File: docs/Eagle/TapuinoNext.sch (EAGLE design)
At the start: 8 parts

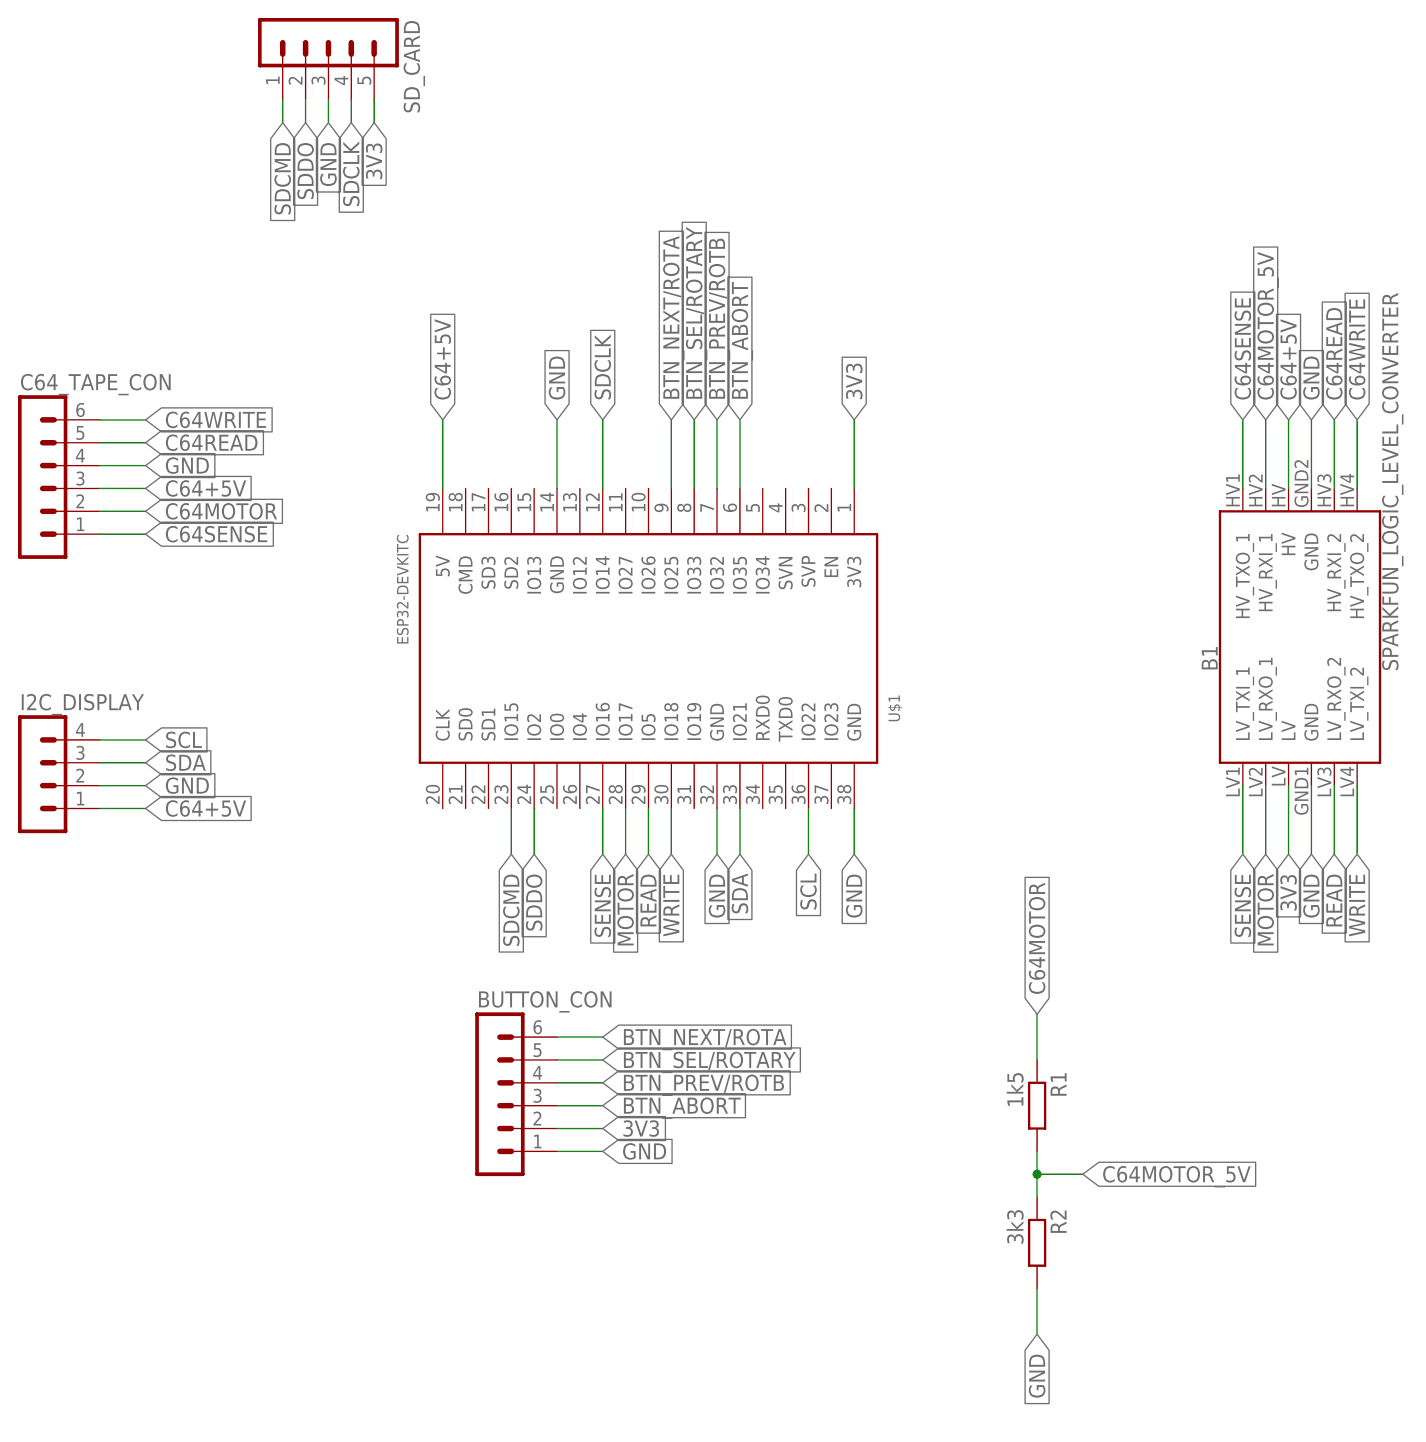
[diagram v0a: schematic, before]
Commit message: add rec led and tidied up the board / schematic
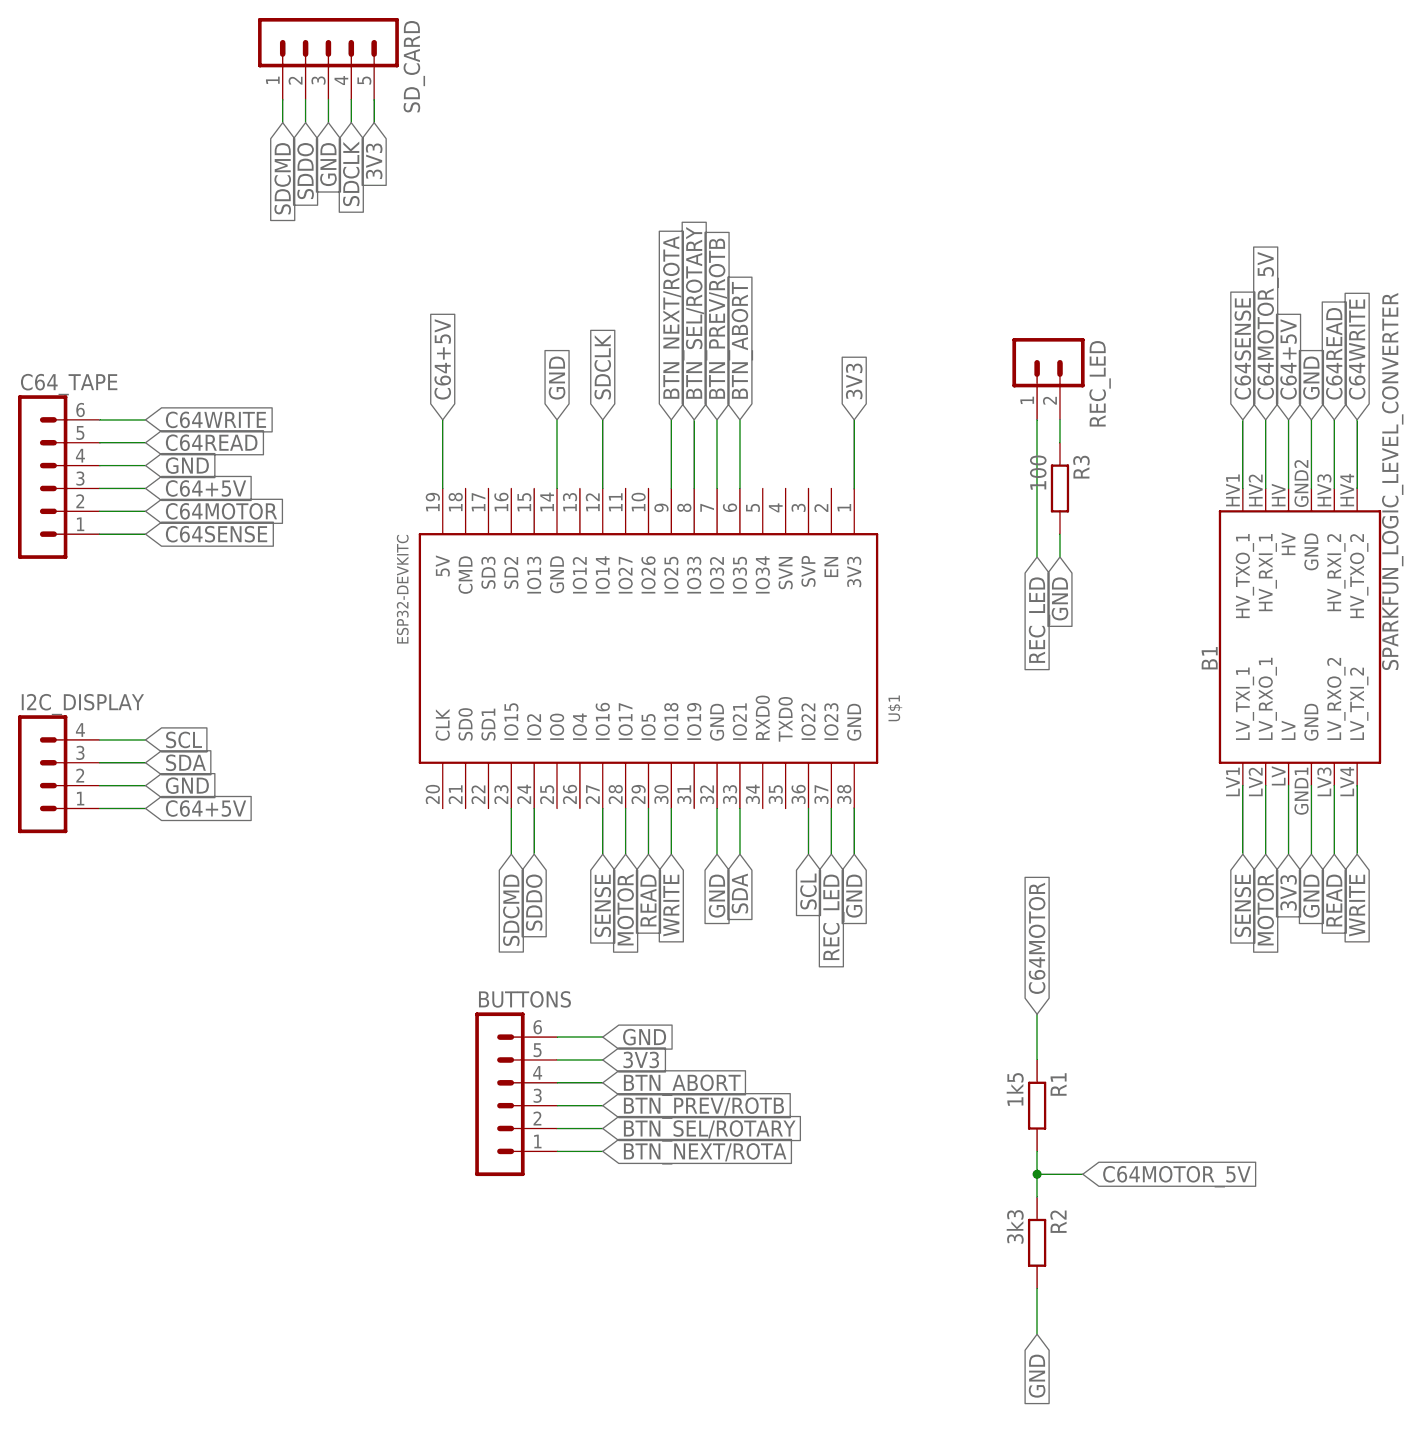
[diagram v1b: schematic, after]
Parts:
- added R3: 100, rcl:R-EU_0204/7
- added REC_LED: (no value), con-lstb-ext:MA02-1
- renumbered BUTTON_CON to BUTTONS, C64_TAPE_CON to C64_TAPE
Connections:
- new net N$2: R3.1, REC_LED.2
- new net REC_LED: REC_LED.1, U$1.IO23
- net 3V3: now also BUTTONS.5; no longer BUTTONS.2
- net BTN_ABORT: now also BUTTONS.4; no longer BUTTONS.3
- net BTN_NEXT/ROTA: now also BUTTONS.1; no longer BUTTONS.6
- net BTN_PREV/ROTB: now also BUTTONS.3; no longer BUTTONS.4
- net BTN_SEL/ROTARY: now also BUTTONS.2; no longer BUTTONS.5
- net GND: now also BUTTONS.6, R3.2; no longer BUTTONS.1
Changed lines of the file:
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@@
 <part name="U$1" library="ESP32-DEVKITC" deviceset="ESP32DEVKITC" device=""/>
 <part name="I2C_DISPLAY" library="con-lstb" library_urn="urn:adsk.eagle:library:162" deviceset="MA04-1" device="" package3d_urn="urn:adsk.eagle:package:8337/1"/>
-<part name="C64_TAPE_CON" library="con-lstb" library_urn="urn:adsk.eagle:library:162" deviceset="MA06-1" device="" package3d_urn="urn:adsk.eagle:package:8340/1"/>
-<part name="BUTTON_CON" library="con-lstb" library_urn="urn:adsk.eagle:library:162" deviceset="MA06-1" device="" package3d_urn="urn:adsk.eagle:package:8340/1"/>
+<part name="C64_TAPE" library="con-lstb" library_urn="urn:adsk.eagle:library:162" deviceset="MA06-1" device="" package3d_urn="urn:adsk.eagle:package:8340/1"/>
+<part name="BUTTONS" library="con-lstb" library_urn="urn:adsk.eagle:library:162" deviceset="MA06-1" device="" package3d_urn="urn:adsk.eagle:package:8340/1"/>
 <part name="R2" library="rcl" library_urn="urn:adsk.eagle:library:334" deviceset="R-EU_" device="0204/7" package3d_urn="urn:adsk.eagle:package:23498/2" value="3k3"/>
 <part name="R1" library="rcl" library_urn="urn:adsk.eagle:library:334" deviceset="R-EU_" device="0204/7" package3d_urn="urn:adsk.eagle:package:23498/2" value="1k5"/>
 <part name="SD_CARD" library="con-lstb" library_urn="urn:adsk.eagle:library:162" deviceset="MA05-1" device="" package3d_urn="urn:adsk.eagle:package:8332/1"/>
+<part name="R3" library="rcl" library_urn="urn:adsk.eagle:library:334" deviceset="R-EU_" device="0204/7" package3d_urn="urn:adsk.eagle:package:23498/2" value="100"/>
+<part name="REC_LED" library="con-lstb-ext" deviceset="MA02-1" device="" package3d_urn="urn:adsk.eagle:package:30404189/1"/>
 </parts>
 <sheets>
@@
 <attribute name="NAME" x="-24.13" y="36.322" size="1.778" layer="95"/>
 </instance>
-<instance part="C64_TAPE_CON" gate="1" x="-22.86" y="63.5" smashed="yes">
+<instance part="C64_TAPE" gate="1" x="-22.86" y="63.5" smashed="yes">
 <attribute name="VALUE" x="-24.13" y="50.8" size="1.778" layer="96"/>
 <attribute name="NAME" x="-24.13" y="71.882" size="1.778" layer="95"/>
 </instance>
-<instance part="BUTTON_CON" gate="1" x="27.94" y="-5.08" smashed="yes">
+<instance part="BUTTONS" gate="1" x="27.94" y="-5.08" smashed="yes">
 <attribute name="VALUE" x="26.67" y="-17.78" size="1.778" layer="96"/>
 <attribute name="NAME" x="26.67" y="3.302" size="1.778" layer="95"/>
@@
 <attribute name="VALUE" x="0" y="113.03" size="1.778" layer="96" rot="R270"/>
 <attribute name="NAME" x="18.542" y="113.03" size="1.778" layer="95" rot="R270"/>
+</instance>
+<instance part="R3" gate="G$1" x="91.44" y="60.96" smashed="yes" rot="R270">
+<attribute name="NAME" x="92.9386" y="64.77" size="1.778" layer="95" rot="R270"/>
+<attribute name="VALUE" x="88.138" y="64.77" size="1.778" layer="96" rot="R270"/>
+</instance>
+<instance part="REC_LED" gate="G$1" x="91.44" y="76.2" smashed="yes" rot="R270">
+<attribute name="VALUE" x="83.82" y="77.47" size="1.778" layer="96" rot="R270"/>
+<attribute name="NAME" x="94.742" y="77.47" size="1.778" layer="95" rot="R270"/>
 </instance>
 </instances>
@@
 <net name="C64SENSE" class="0">
 <segment>
-<pinref part="C64_TAPE_CON" gate="1" pin="1"/>
+<pinref part="C64_TAPE" gate="1" pin="1"/>
 <wire x1="-15.24" y1="55.88" x2="-10.16" y2="55.88" width="0.1524" layer="91"/>
 <label x="-10.16" y="55.88" size="1.778" layer="95" xref="yes"/>
@@
 <net name="C64MOTOR" class="0">
 <segment>
-<pinref part="C64_TAPE_CON" gate="1" pin="2"/>
+<pinref part="C64_TAPE" gate="1" pin="2"/>
 <wire x1="-15.24" y1="58.42" x2="-10.16" y2="58.42" width="0.1524" layer="91"/>
 <label x="-10.16" y="58.42" size="1.778" layer="95" xref="yes"/>
@@
 <net name="C64+5V" class="0">
 <segment>
-<pinref part="C64_TAPE_CON" gate="1" pin="3"/>
+<pinref part="C64_TAPE" gate="1" pin="3"/>
 <wire x1="-15.24" y1="60.96" x2="-10.16" y2="60.96" width="0.1524" layer="91"/>
 <label x="-10.16" y="60.96" size="1.778" layer="95" xref="yes"/>
@@
 <net name="GND" class="0">
 <segment>
-<pinref part="C64_TAPE_CON" gate="1" pin="4"/>
+<pinref part="C64_TAPE" gate="1" pin="4"/>
 <wire x1="-15.24" y1="63.5" x2="-10.16" y2="63.5" width="0.1524" layer="91"/>
 <label x="-10.16" y="63.5" size="1.778" layer="95" xref="yes"/>
@@
 </segment>
 <segment>
-<pinref part="BUTTON_CON" gate="1" pin="1"/>
-<wire x1="35.56" y1="-12.7" x2="40.64" y2="-12.7" width="0.1524" layer="91"/>
-<label x="40.64" y="-12.7" size="1.778" layer="95" xref="yes"/>
-</segment>
-<segment>
 <pinref part="R2" gate="G$1" pin="2"/>
 <wire x1="88.9" y1="-27.94" x2="88.9" y2="-33.02" width="0.1524" layer="91"/>
@@
 <label x="-10.16" y="27.94" size="1.778" layer="95" xref="yes"/>
 </segment>
+<segment>
+<pinref part="R3" gate="G$1" pin="2"/>
+<wire x1="91.44" y1="55.88" x2="91.44" y2="53.34" width="0.1524" layer="91"/>
+<label x="91.44" y="53.34" size="1.778" layer="95" rot="R270" xref="yes"/>
+</segment>
+<segment>
+<pinref part="BUTTONS" gate="1" pin="6"/>
+<wire x1="35.56" y1="0" x2="40.64" y2="0" width="0.1524" layer="91"/>
+<label x="40.64" y="0" size="1.778" layer="95" xref="yes"/>
+</segment>
 </net>
 <net name="C64READ" class="0">
 <segment>
-<pinref part="C64_TAPE_CON" gate="1" pin="5"/>
+<pinref part="C64_TAPE" gate="1" pin="5"/>
 <wire x1="-15.24" y1="66.04" x2="-10.16" y2="66.04" width="0.1524" layer="91"/>
 <label x="-10.16" y="66.04" size="1.778" layer="95" xref="yes"/>
@@
 <net name="C64WRITE" class="0">
 <segment>
-<pinref part="C64_TAPE_CON" gate="1" pin="6"/>
+<pinref part="C64_TAPE" gate="1" pin="6"/>
 <wire x1="-15.24" y1="68.58" x2="-10.16" y2="68.58" width="0.1524" layer="91"/>
 <label x="-10.16" y="68.58" size="1.778" layer="95" xref="yes"/>
@@
 </segment>
 <segment>
-<pinref part="BUTTON_CON" gate="1" pin="2"/>
-<wire x1="35.56" y1="-10.16" x2="40.64" y2="-10.16" width="0.1524" layer="91"/>
-<label x="40.64" y="-10.16" size="1.778" layer="95" xref="yes"/>
-</segment>
-<segment>
 <pinref part="SD_CARD" gate="G$1" pin="5"/>
 <wire x1="15.24" y1="104.14" x2="15.24" y2="101.6" width="0.1524" layer="91"/>
 <label x="15.24" y="101.6" size="1.778" layer="95" rot="R270" xref="yes"/>
 </segment>
+<segment>
+<pinref part="BUTTONS" gate="1" pin="5"/>
+<wire x1="35.56" y1="-2.54" x2="40.64" y2="-2.54" width="0.1524" layer="91"/>
+<label x="40.64" y="-2.54" size="1.778" layer="95" xref="yes"/>
+</segment>
 </net>
 <net name="SDDO" class="0">
@@
 <net name="BTN_ABORT" class="0">
 <segment>
-<pinref part="BUTTON_CON" gate="1" pin="3"/>
-<wire x1="35.56" y1="-7.62" x2="40.64" y2="-7.62" width="0.1524" layer="91"/>
-<label x="40.64" y="-7.62" size="1.778" layer="95" xref="yes"/>
-</segment>
-<segment>
 <pinref part="U$1" gate="G$1" pin="IO35"/>
 <wire x1="55.88" y1="60.96" x2="55.88" y2="68.58" width="0.1524" layer="91"/>
 <label x="55.88" y="68.58" size="1.778" layer="95" rot="R90" xref="yes"/>
 </segment>
-</net>
-<net name="BTN_PREV/ROTB" class="0">
-<segment>
-<pinref part="BUTTON_CON" gate="1" pin="4"/>
+<segment>
+<pinref part="BUTTONS" gate="1" pin="4"/>
 <wire x1="35.56" y1="-5.08" x2="40.64" y2="-5.08" width="0.1524" layer="91"/>
 <label x="40.64" y="-5.08" size="1.778" layer="95" xref="yes"/>
 </segment>
+</net>
+<net name="BTN_PREV/ROTB" class="0">
 <segment>
 <pinref part="U$1" gate="G$1" pin="IO32"/>
@@
 <label x="53.34" y="68.58" size="1.778" layer="95" rot="R90" xref="yes"/>
 </segment>
+<segment>
+<pinref part="BUTTONS" gate="1" pin="3"/>
+<wire x1="35.56" y1="-7.62" x2="40.64" y2="-7.62" width="0.1524" layer="91"/>
+<label x="40.64" y="-7.62" size="1.778" layer="95" xref="yes"/>
+</segment>
 </net>
 <net name="BTN_SEL/ROTARY" class="0">
-<segment>
-<pinref part="BUTTON_CON" gate="1" pin="5"/>
-<wire x1="35.56" y1="-2.54" x2="40.64" y2="-2.54" width="0.1524" layer="91"/>
-<label x="40.64" y="-2.54" size="1.778" layer="95" xref="yes"/>
-</segment>
 <segment>
 <pinref part="U$1" gate="G$1" pin="IO33"/>
@@
 <label x="50.8" y="68.58" size="1.778" layer="95" rot="R90" xref="yes"/>
 </segment>
+<segment>
+<pinref part="BUTTONS" gate="1" pin="2"/>
+<wire x1="35.56" y1="-10.16" x2="40.64" y2="-10.16" width="0.1524" layer="91"/>
+<label x="40.64" y="-10.16" size="1.778" layer="95" xref="yes"/>
+</segment>
 </net>
 <net name="BTN_NEXT/ROTA" class="0">
-<segment>
-<pinref part="BUTTON_CON" gate="1" pin="6"/>
-<wire x1="35.56" y1="0" x2="40.64" y2="0" width="0.1524" layer="91"/>
-<label x="40.64" y="0" size="1.778" layer="95" xref="yes"/>
-</segment>
 <segment>
 <pinref part="U$1" gate="G$1" pin="IO25"/>
 <wire x1="48.26" y1="60.96" x2="48.26" y2="68.58" width="0.1524" layer="91"/>
 <label x="48.26" y="68.58" size="1.778" layer="95" rot="R90" xref="yes"/>
+</segment>
+<segment>
+<pinref part="BUTTONS" gate="1" pin="1"/>
+<wire x1="35.56" y1="-12.7" x2="40.64" y2="-12.7" width="0.1524" layer="91"/>
+<label x="40.64" y="-12.7" size="1.778" layer="95" xref="yes"/>
 </segment>
 </net>
@@
 </segment>
 </net>
+<net name="REC_LED" class="0">
+<segment>
+<pinref part="U$1" gate="G$1" pin="IO23"/>
+<wire x1="66.04" y1="25.4" x2="66.04" y2="20.32" width="0.1524" layer="91"/>
+<label x="66.04" y="20.32" size="1.778" layer="95" rot="R270" xref="yes"/>
+</segment>
+<segment>
+<pinref part="REC_LED" gate="G$1" pin="1"/>
+<wire x1="88.9" y1="68.58" x2="88.9" y2="53.34" width="0.1524" layer="91"/>
+<label x="88.9" y="53.34" size="1.778" layer="95" rot="R270" xref="yes"/>
+</segment>
+</net>
+<net name="N$2" class="0">
+<segment>
+<pinref part="REC_LED" gate="G$1" pin="2"/>
+<wire x1="91.44" y1="68.58" x2="91.44" y2="66.04" width="0.1524" layer="91"/>
+<pinref part="R3" gate="G$1" pin="1"/>
+</segment>
+</net>
